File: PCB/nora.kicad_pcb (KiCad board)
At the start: 2 copper layers, 285 x 95.1 mm, 219 parts, among them J1 USB_C_Receptacle_USB2.0, J2 Conn_01x04, J3 Conn_01x02, J5 Conn_02x03_Odd_Even, U1 ATmega32U4-MU, U2 24LC64, U4 Pico, Y1 16MHz

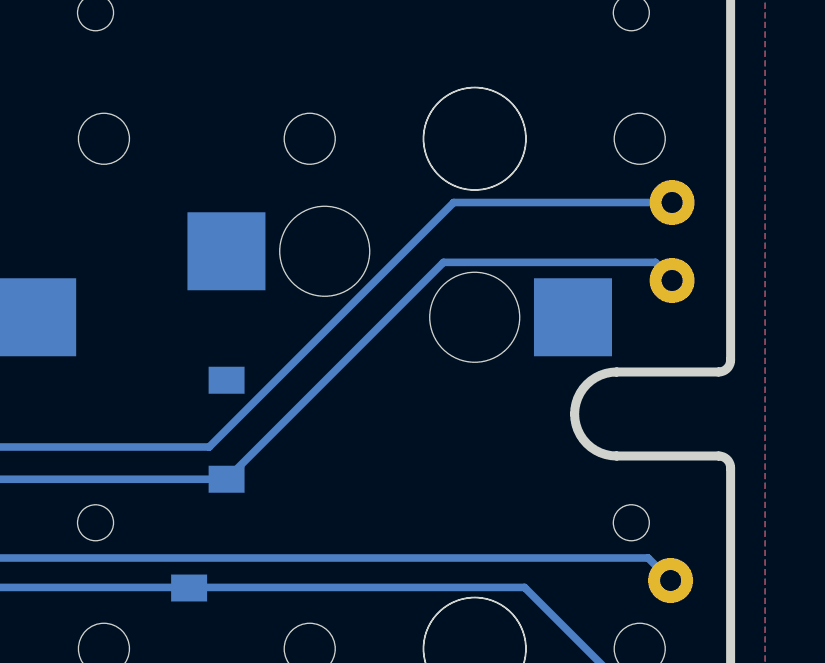
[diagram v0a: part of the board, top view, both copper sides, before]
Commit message: WIP パーツ配置。EEPROM配置中。
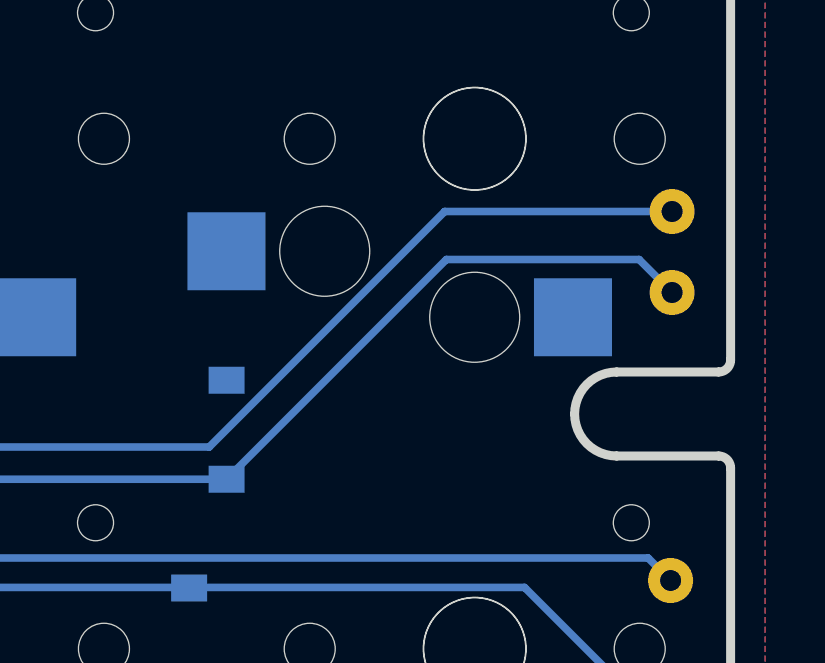
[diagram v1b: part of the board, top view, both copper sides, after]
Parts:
- moved EXT_R7 0.40 mm to (305.6, 75.0)
- moved EXT_R2 0.30 mm to (305.6, 72.3)
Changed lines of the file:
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@@
   )
   (module TestPoint:TestPoint_THTPad_D1.5mm_Drill0.7mm (layer B.Cu)
-    (at 305.649984 72 90)
+    (at 305.649984 72.3 90)
     (descr "THT pad as test Point, diameter 1.5mm, hole diameter 0.7mm")
     (tags "test point THT pad")
@@
   )
   (module TestPoint:TestPoint_THTPad_D1.5mm_Drill0.7mm (layer B.Cu)
-    (at 305.65 74.6 270)
+    (at 305.65 75 270)
     (descr "THT pad as test Point, diameter 1.5mm, hole diameter 0.7mm")
     (tags "test point THT pad")
@@
   (segment (start 268.497738 81.225) (end 290.8 81.225) (width 0.254) (layer B.Cu) (net 80))
   (segment (start 255 81.225) (end 268.497738 81.225) (width 0.254) (layer B.Cu) (net 80))
-  (segment (start 305.095319 73.995319) (end 305.7 74.6) (width 0.254) (layer B.Cu) (net 80))
-  (segment (start 298.029681 73.995319) (end 305.095319 73.995319) (width 0.254) (layer B.Cu) (net 80))
-  (segment (start 290.8 81.225) (end 298.029681 73.995319) (width 0.254) (layer B.Cu) (net 80))
   (segment (start 25.25 74.75) (end 24.2 74.75) (width 0.254) (layer B.Cu) (net 80))
   (segment (start 28.155721 77.655721) (end 25.25 74.75) (width 0.254) (layer B.Cu) (net 80))
@@
   (segment (start 52.72552 81.22552) (end 49.155721 77.655721) (width 0.254) (layer B.Cu) (net 80))
   (segment (start 67.549984 81.22552) (end 52.72552 81.22552) (width 0.254) (layer B.Cu) (net 80))
+  (segment (start 304.55 73.9) (end 305.65 75) (width 0.254) (layer B.Cu) (net 80))
+  (segment (start 298.125 73.9) (end 304.55 73.9) (width 0.254) (layer B.Cu) (net 80))
+  (segment (start 290.8 81.225) (end 298.125 73.9) (width 0.254) (layer B.Cu) (net 80))
   (segment (start 110.92552 84.82552) (end 110.95 84.85) (width 0.254) (layer B.Cu) (net 83))
   (segment (start 75.349984 84.82552) (end 110.92552 84.82552) (width 0.254) (layer B.Cu) (net 83))
@@
   (segment (start 192.5 80.15) (end 232.7 80.15) (width 0.254) (layer B.Cu) (net 88))
   (segment (start 232.7 80.15) (end 272.9 80.15) (width 0.254) (layer B.Cu) (net 88))
-  (segment (start 298.369362 72) (end 305.649984 72) (width 0.254) (layer B.Cu) (net 88))
-  (segment (start 290.219362 80.15) (end 298.369362 72) (width 0.254) (layer B.Cu) (net 88))
-  (segment (start 272.9 80.15) (end 290.219362 80.15) (width 0.254) (layer B.Cu) (net 88))
   (segment (start 85.349464 80.125) (end 85.349984 80.12552) (width 0.254) (layer B.Cu) (net 88))
   (segment (start 64.7 80.125) (end 85.349464 80.125) (width 0.254) (layer B.Cu) (net 88))
@@
   (segment (start 49.549984 64.77552) (end 50.265939 64.77552) (width 0.254) (layer B.Cu) (net 88))
   (segment (start 50.7 65.209581) (end 50.7 67.7) (width 0.254) (layer B.Cu) (net 88))
+  (segment (start 298.069362 72.3) (end 305.649984 72.3) (width 0.254) (layer B.Cu) (net 88))
+  (segment (start 290.219362 80.15) (end 298.069362 72.3) (width 0.254) (layer B.Cu) (net 88))
+  (segment (start 272.9 80.15) (end 290.219362 80.15) (width 0.254) (layer B.Cu) (net 88))
   (segment (start 49.549984 65.27552) (end 50.119347 65.27552) (width 0.254) (layer B.Cu) (net 103))
   (segment (start 50.119347 65.27552) (end 50.242789 65.398962) (width 0.254) (layer B.Cu) (net 103))

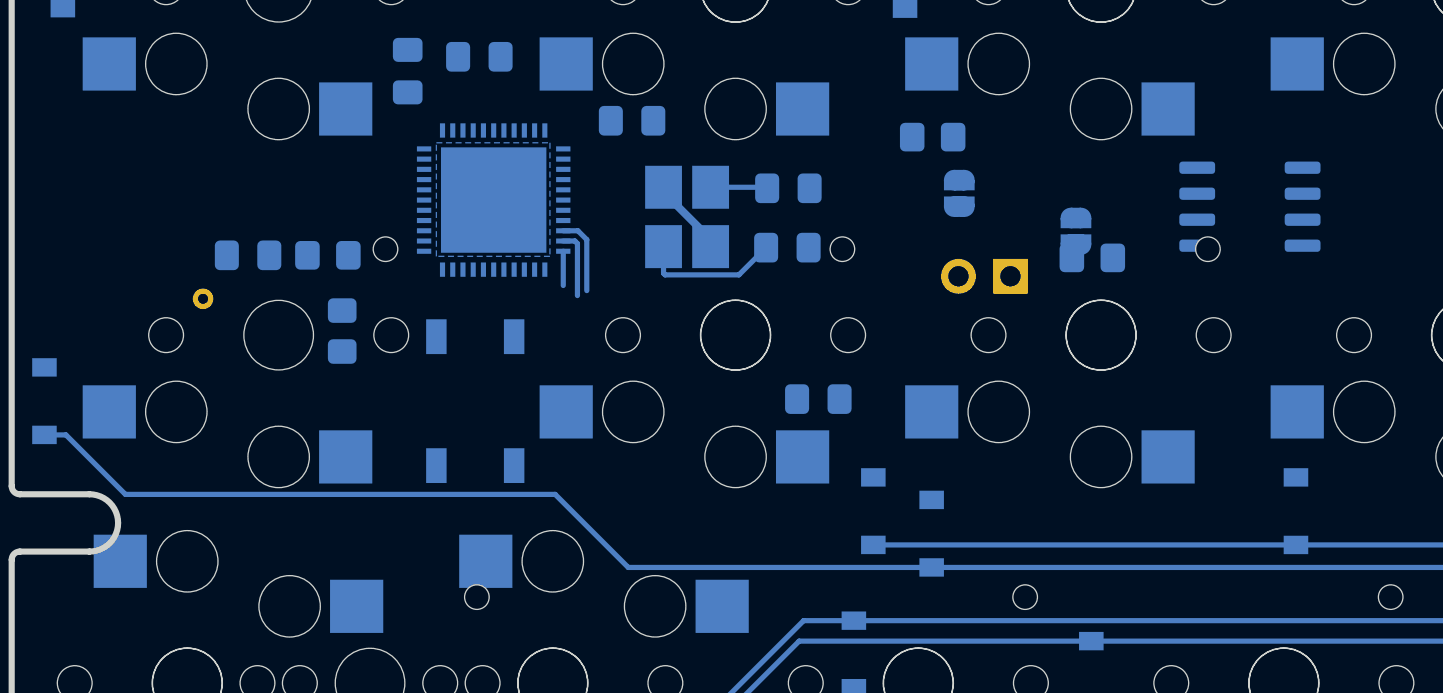
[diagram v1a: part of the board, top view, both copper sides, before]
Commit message: WIP EEPROM、I2C、とりあえず完了
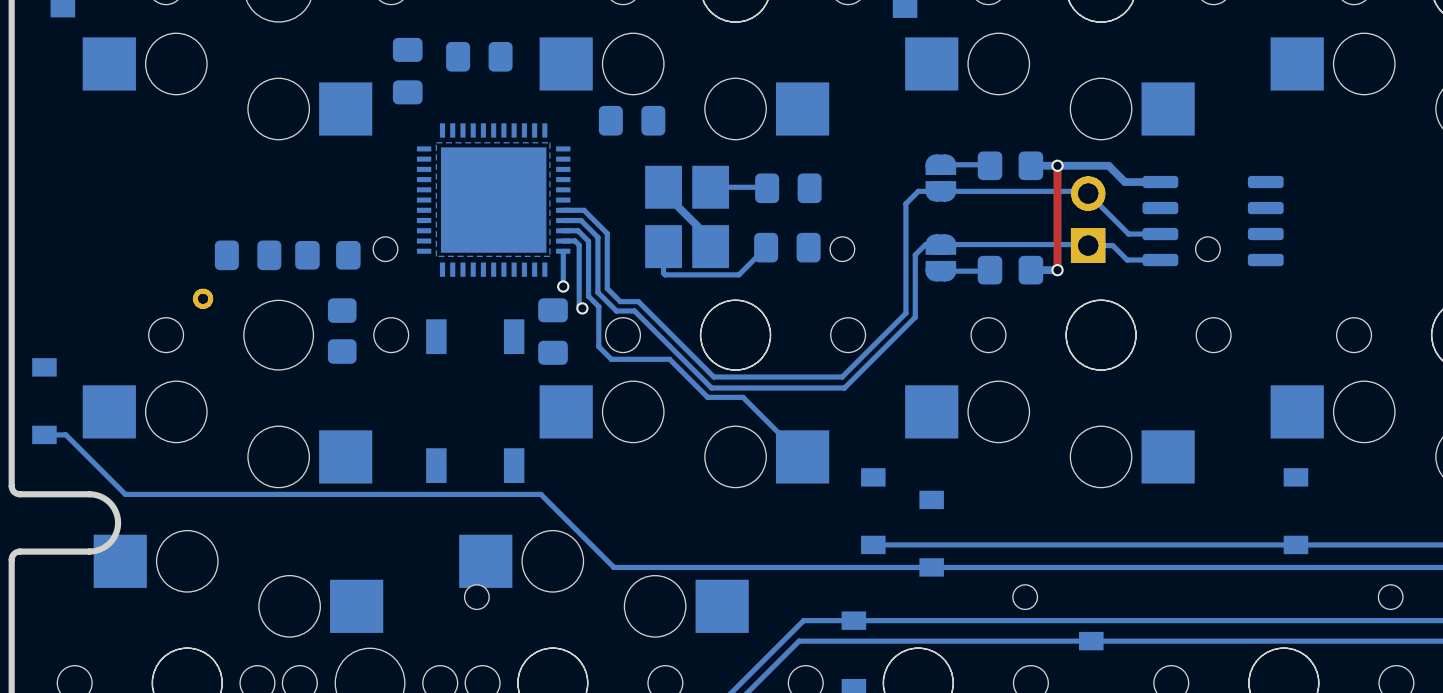
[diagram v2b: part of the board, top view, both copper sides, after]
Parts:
- moved C4 13.4 mm to (49.0, 69.7), turned to 90 degrees
- moved JP1 6.73 mm to (68.0, 66.1)
- moved J3 4.09 mm to (75.2, 65.5), turned to 0 degrees
- moved R9 4.05 mm to (71.4, 61.6), turned to 180 degrees
- moved R8 4.04 mm to (71.4, 66.7)
- moved U2 1.93 mm to (81.3, 64.3)
- moved JP2 1.17 mm to (68.0, 62.2)
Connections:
- U1 pad 20: row2 -> col1
- U1 pad 21: col1 -> row2
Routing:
- net SCL: track 0.00 -> 41.9 mm
- net SDA: track 0.00 -> 39.1 mm
- net col1: track 3.29 -> 19.0 mm
- net +5V: track 0.00 -> 13.1 mm, vias 0 -> 2
- net Net-(JP2-Pad1): track 0.00 -> 2.42 mm
- net Net-(JP1-Pad1): track 0.00 -> 2.42 mm
- net row2: track 248.0 -> 248.2 mm, vias 0 -> 1
- net col2: track 1.67 -> 1.72 mm, vias 0 -> 1

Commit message: WIP 怪しそうなところを配線中
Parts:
- moved Ext_PC6 8.66 mm to (40.6, 67.6)
- moved JP3 1.57 mm to (60.2, 26.9)
- moved C7 0.75 mm to (52.6, 60.1)
- moved R4 0.71 mm to (43.1, 33.2)
- moved C6 0.35 mm to (45.1, 56.3)
- moved C4 0.25 mm to (49.3, 69.7)
- moved R5 0.15 mm to (38.6, 69.7)
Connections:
- U1 pad 30: row9 -> row8
- U1 pad 32: row8 -> row9
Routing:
- net +5V: track 13.1 -> 89.5 mm, vias 2 -> 9
- net MOSI: track 0.00 -> 60.0 mm, vias 0 -> 3
- net MISO: track 0.00 -> 57.2 mm, vias 0 -> 3
- net SCK: track 0.00 -> 56.6 mm, vias 0 -> 3
- net GND: track 274.3 -> 310.1 mm
- net LED: track 0.00 -> 31.5 mm, vias 0 -> 2
- net D+: track 0.00 -> 31.0 mm, vias 0 -> 2
- net RESET: track 0.00 -> 30.4 mm, vias 0 -> 4
- net D-: track 0.00 -> 27.7 mm, vias 0 -> 2
- net row5: track 268.6 -> 282.4 mm, vias 0 -> 2
- net VCC: track 0.00 -> 10.3 mm
- net Net-(C3-Pad1): track 2.78 -> 11.3 mm
- net Net-(D10-Pad3): track 0.00 -> 8.38 mm
- net Net-(JP3-Pad2): track 291.8 -> 298.0 mm, vias 0 -> 2
- net Reserve_pin: track 0.00 -> 5.29 mm
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
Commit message: WIP 怪しそうなところを配線中
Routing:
- net col0: track 0.00 -> 112.9 mm, vias 0 -> 9
- net row4: track 275.0 -> 334.3 mm, vias 0 -> 2
- net GND: track 310.1 -> 315.9 mm

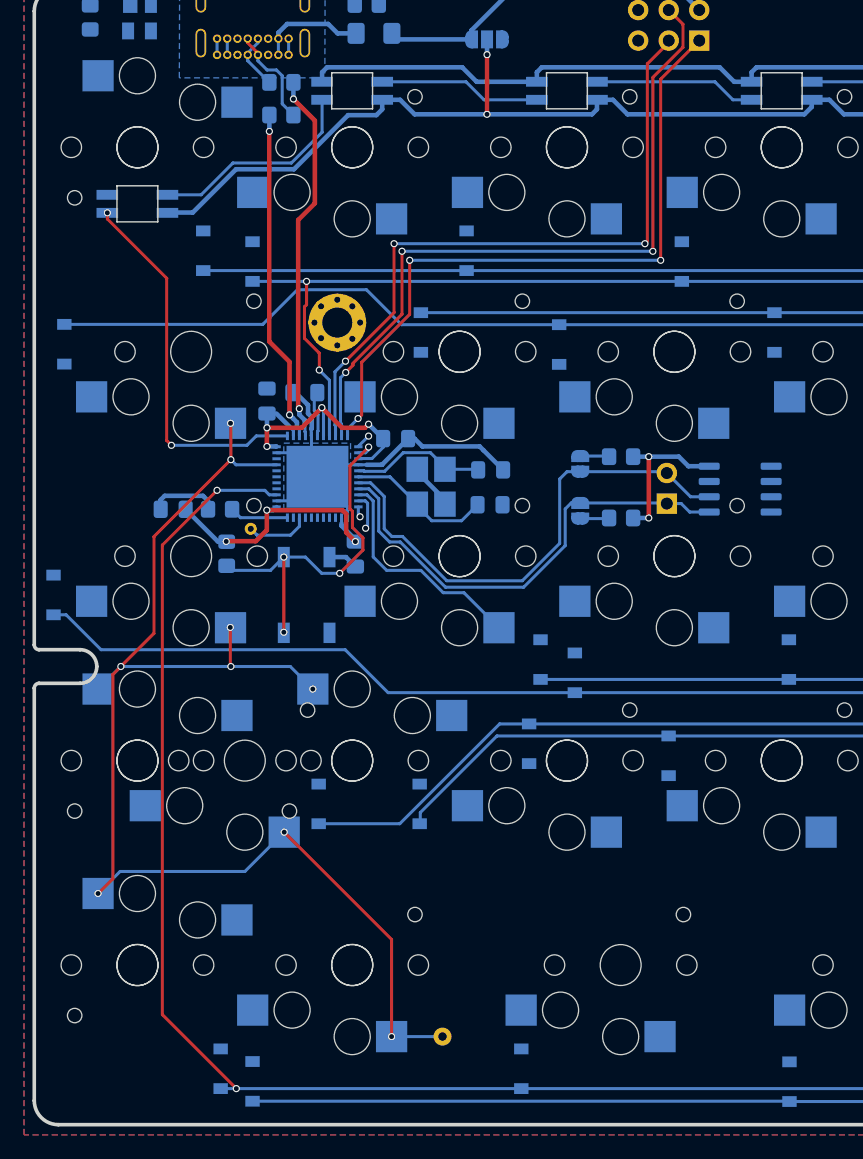
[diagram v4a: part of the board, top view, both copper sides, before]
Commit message: ソケット化と、関連するパーツの配置と配線に目処が立つ#1
FULL hotswap socket support
Fixes #1
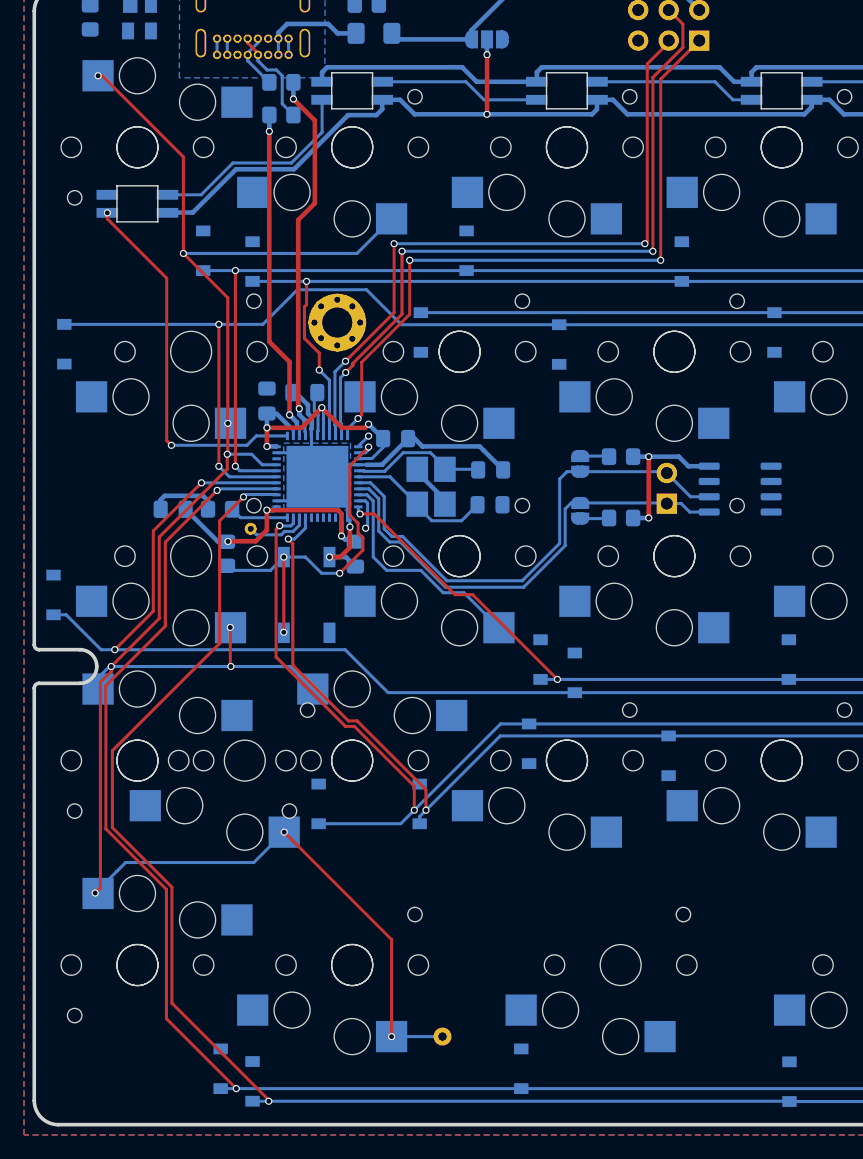
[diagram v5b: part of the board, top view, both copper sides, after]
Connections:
- U1 pad 21: row2 -> col2
- U1 pad 22: col2 -> row2
- U1 pad 32: row9 -> row3
- U1 pad 36: row4 -> row9
- U1 pad 37: row3 -> row4
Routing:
- net row9: track 267.3 -> 330.3 mm, vias 0 -> 2
- net col0: track 112.9 -> 166.2 mm, vias 9 -> 10
- net row3: track 263.1 -> 293.8 mm, vias 0 -> 2
- net row8: track 256.6 -> 286.8 mm, vias 0 -> 2
- net row7: track 287.6 -> 310.8 mm, vias 0 -> 2
- net row0: track 274.6 -> 294.4 mm, vias 0 -> 2
- net row2: track 247.2 -> 267.0 mm, vias 1 -> 2
- net row6: track 288.9 -> 305.9 mm, vias 0 -> 2
- net GND: track 315.9 -> 320.5 mm, vias 0 -> 2
- net row4: track 334.3 -> 338.1 mm
- net col2: track 0.88 -> 3.00 mm
- net +5V: track 89.5 -> 88.9 mm

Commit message: WIP 回路図へLED追加。とりあえずPCBへ配置
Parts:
- added L17: SK6812MINI-E, Jones.local:YS-SK6812MINI-E, B.Cu at (299.1, 99.2)
- added L18: SK6812MINI-E, Jones.local:YS-SK6812MINI-E, B.Cu at (281.2, 99.2)
- added L19: SK6812MINI-E, Jones.local:YS-SK6812MINI-E, B.Cu at (263.3, 103.4)
- added L20: SK6812MINI-E, Jones.local:YS-SK6812MINI-E, B.Cu at (245.5, 103.4)
- added L21: SK6812MINI-E, Jones.local:YS-SK6812MINI-E, B.Cu at (227.6, 103.4)
- added L22: SK6812MINI-E, Jones.local:YS-SK6812MINI-E, B.Cu at (205.3, 99.2)
- added L23: SK6812MINI-E, Jones.local:YS-SK6812MINI-E, B.Cu at (183.0, 99.2)
- added L24: SK6812MINI-E, Jones.local:YS-SK6812MINI-E, B.Cu at (156.2, 99.2)
- added L25: SK6812MINI-E, Jones.local:YS-SK6812MINI-E, B.Cu at (120.5, 99.2)
- added L26: SK6812MINI-E, Jones.local:YS-SK6812MINI-E, B.Cu at (93.7, 99.2)
- added L27: SK6812MINI-E, Jones.local:YS-SK6812MINI-E, B.Cu at (71.4, 99.2)
- added L28: SK6812MINI-E, Jones.local:YS-SK6812MINI-E, B.Cu at (49.0, 99.2)
- added L29: SK6812MINI-E, Jones.local:YS-SK6812MINI-E, B.Cu at (31.2, 108.6)
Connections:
- net Net-(JP3-Pad2) renamed LED_VDD
- L16 pad 2: (no net) -> LED_connection

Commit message: R5へのLED配置、配線完了#3 Full RGB LED backlight Fixes #3
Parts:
- turned L17 to 180 degrees
- turned L18 to 180 degrees
- turned L19 to 180 degrees
- turned L20 to 180 degrees
- turned L21 to 180 degrees
- turned L22 to 180 degrees
- turned L23 to 180 degrees
- turned L24 to 180 degrees
- turned L25 to 180 degrees
- turned L26 to 180 degrees
- turned L27 to 180 degrees
- turned L28 to 180 degrees
- turned L29 to 180 degrees
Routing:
- net LED_VDD: track 298.0 -> 654.6 mm, vias 2 -> 4
- net GND: track 320.5 -> 612.4 mm
- net LED_connection: track 0.00 -> 76.7 mm, vias 0 -> 2
- net Net-(L24-Pad2): track 0.00 -> 31.3 mm
- net Net-(L23-Pad2): track 0.00 -> 22.4 mm
- net Net-(L25-Pad2): track 0.00 -> 22.4 mm
- net Net-(L21-Pad2): track 0.00 -> 19.7 mm
- net Net-(L27-Pad2): track 0.00 -> 17.9 mm
- net Net-(L26-Pad2): track 0.00 -> 17.9 mm
- net Net-(L22-Pad2): track 0.00 -> 17.9 mm
- net Net-(L28-Pad2): track 0.00 -> 16.1 mm
- net Net-(L18-Pad2): track 0.00 -> 14.0 mm
- net Net-(L20-Pad2): track 0.00 -> 13.5 mm
- net Net-(L19-Pad2): track 0.00 -> 13.5 mm
- net Net-(L17-Pad2): track 0.00 -> 13.5 mm
